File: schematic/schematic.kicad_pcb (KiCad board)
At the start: 4 copper layers, 100 x 100 mm, 260 parts, among them J1 Conn_01x04, J10 Conn_01x03, J11 Conn_01x02, J12 Conn_01x02, J13 Conn_01x02, J14 Conn_01x02, J15 Conn_01x02, J16 Conn_01x02, J17 Conn_01x04, J18 Conn_02x13_Odd_Even, J2 Conn_01x04, J3 Conn_01x04, J4 Conn_01x04, J5 Conn_01x04, J6 Conn_01x06, J7 Conn_01x03, J8 Screw_Terminal_01x02, J9 Conn_01x03, Q1 PSMN1R7-30YL, Q2 PSMN1R7-30YL, Q3 NCV8402, Q4 NCV8402, SW1 SW_Push_Dual, SW2 SW_DIP_x03, U1 STM32F401VETx, U2 TMC2130, U3 TMC2130, U4 TMC2130, U5 TMC2130, U6 BD9E302EFJ, U7 BD9E302EFJ, U8 BD9E302EFJ, Y1 Crystal_GND24

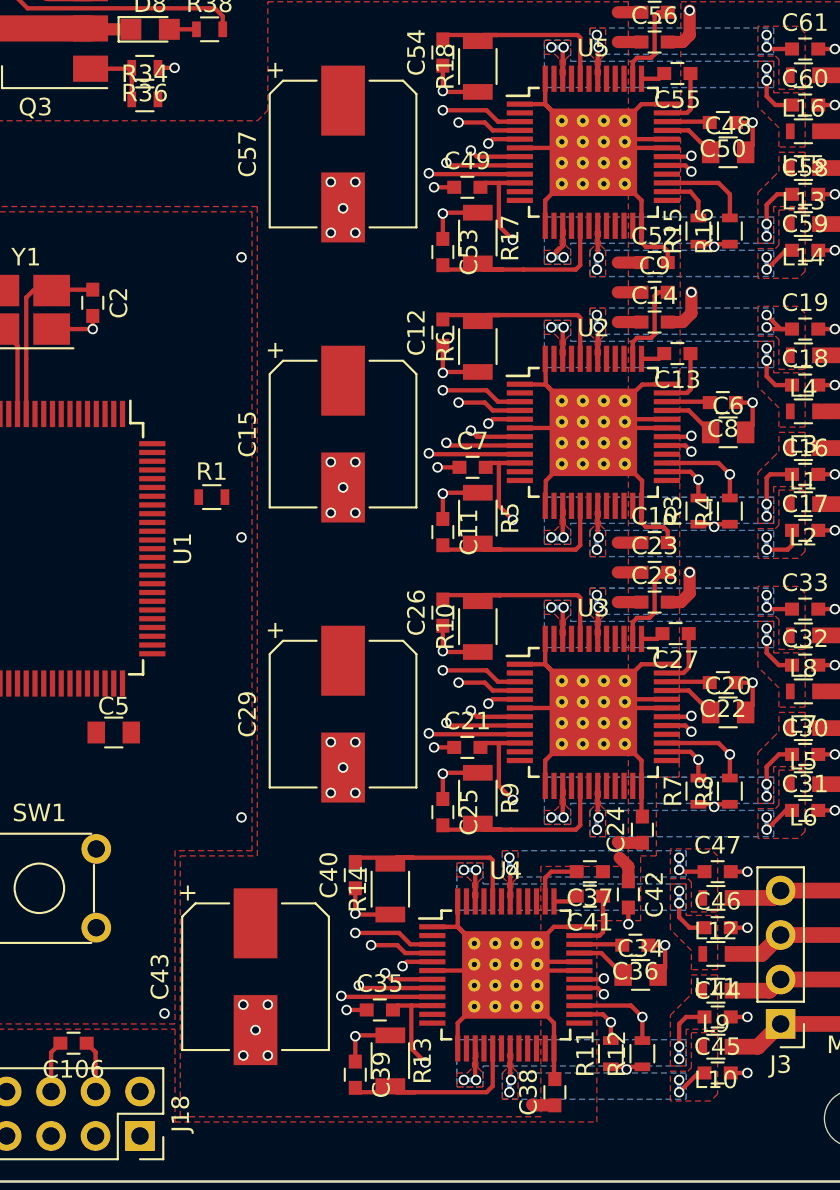
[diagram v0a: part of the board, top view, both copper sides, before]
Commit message: Routed signals to E driver
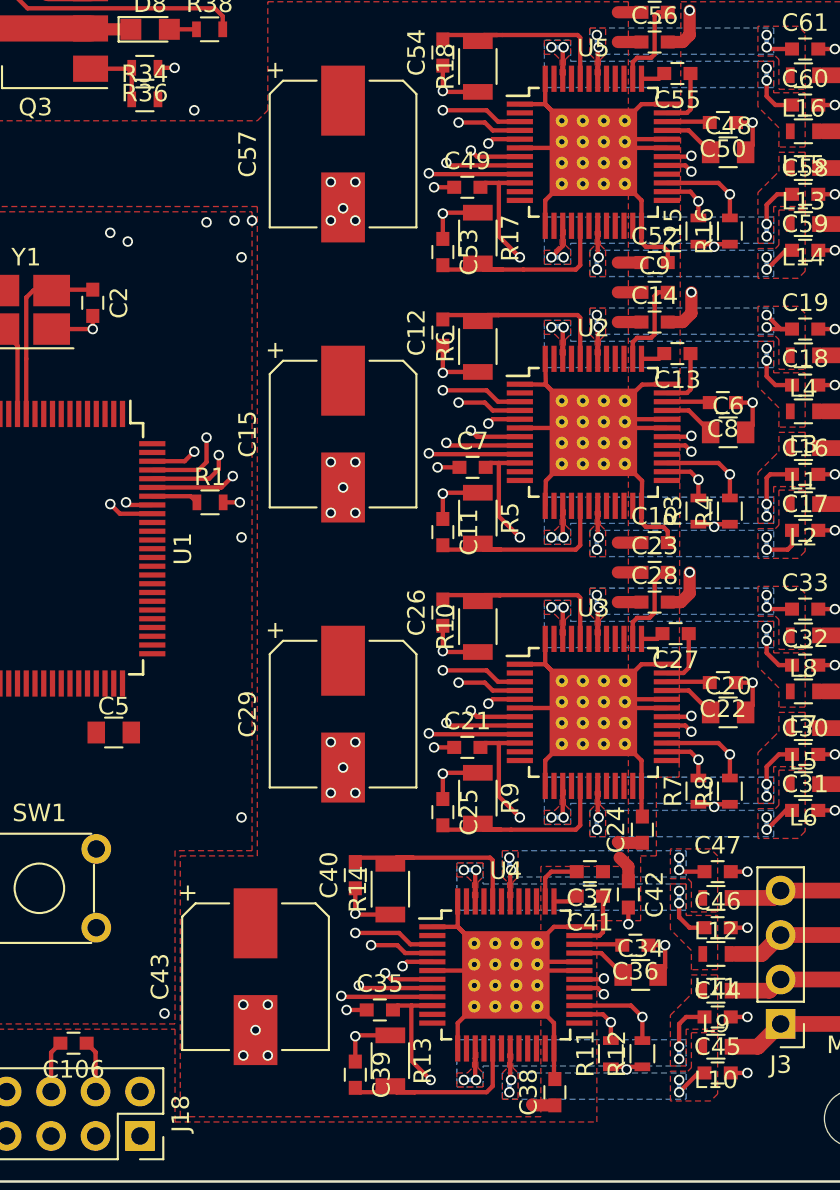
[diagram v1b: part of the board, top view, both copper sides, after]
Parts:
- moved R1 0.32 mm to (224.7, 111.2)
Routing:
- net ED0: track 3.01 -> 55.7 mm, vias 0 -> 3
- net ED1: track 5.22 -> 57.2 mm, vias 0 -> 3
- net ESS: track 4.67 -> 41.0 mm, vias 1 -> 3
- net ESTEP: track 4.26 -> 36.8 mm, vias 1 -> 3
- net EDIR: track 5.22 -> 36.5 mm, vias 1 -> 3
- net EEN: track 17.8 -> 48.4 mm, vias 1 -> 3
- net +3V3: track 144.6 -> 149.5 mm
- net BOOT0: track 0.00 -> 2.69 mm
- net GND: track 362.8 -> 362.6 mm, vias 110 -> 111

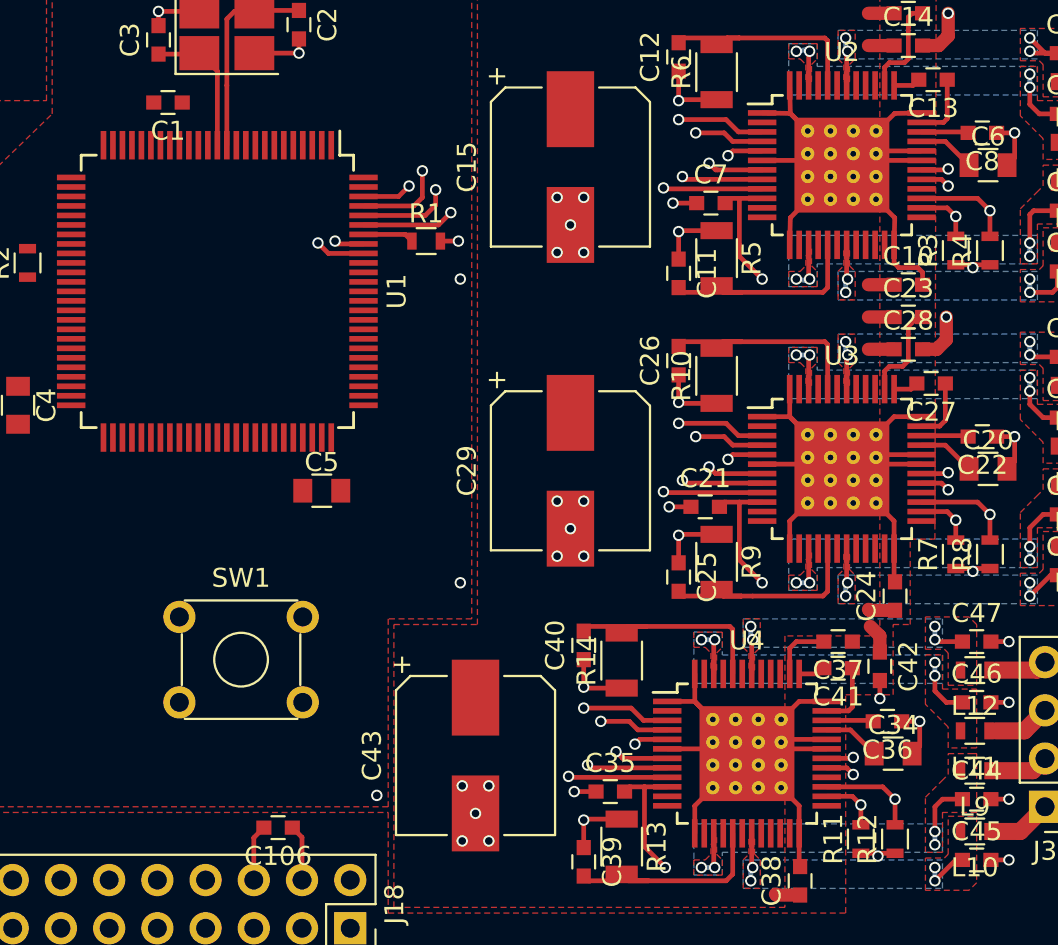
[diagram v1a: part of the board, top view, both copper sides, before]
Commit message: Routed all control signals to drivers
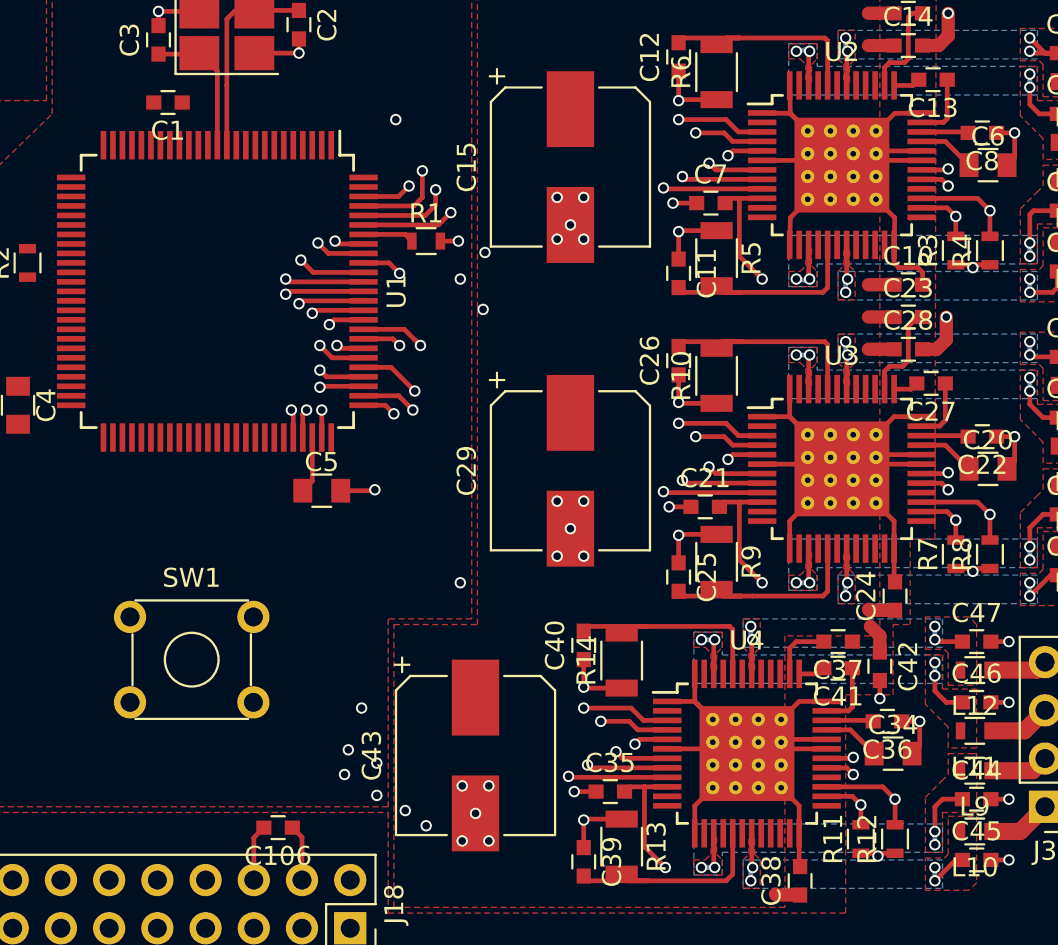
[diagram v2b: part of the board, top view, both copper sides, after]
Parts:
- moved SW1 2.60 mm to (209.1, 131.0)
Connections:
- U1 pad 80: YD0 -> YD1
- U1 pad 81: YD1 -> YD0
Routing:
- net ZD1: track 5.22 -> 60.6 mm, vias 1 -> 3
- net ZD0: track 3.04 -> 55.5 mm, vias 1 -> 3
- net ZEN: track 1.54 -> 51.6 mm, vias 1 -> 3
- net YD0: track 3.04 -> 46.1 mm, vias 1 -> 2
- net XD1: track 5.22 -> 47.1 mm, vias 1 -> 2
- net XEN: track 1.54 -> 43.2 mm, vias 1 -> 2
- net XD0: track 3.04 -> 43.7 mm, vias 1 -> 4
- net YD1: track 5.22 -> 45.3 mm, vias 1 -> 2
- net YEN: track 1.54 -> 41.0 mm, vias 1 -> 2
- net ZSTEP: track 4.26 -> 39.9 mm, vias 1 -> 3
- net ZSS: track 4.67 -> 38.5 mm, vias 1 -> 3
- net ZDIR: track 5.22 -> 37.9 mm, vias 1 -> 3
- net XSTEP: track 4.26 -> 34.8 mm, vias 1 -> 2
- net XDIR: track 5.22 -> 31.8 mm, vias 1 -> 2
- net XSS: track 4.67 -> 30.0 mm, vias 1 -> 3
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
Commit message: More routing done
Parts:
- moved R66 104.2 mm to (239.7, 153.9)
- moved R67 104.2 mm to (243.5, 153.9)
- moved R68 104.2 mm to (247.3, 163.9)
- moved R69 104.2 mm to (243.5, 163.9)
- moved R71 104.2 mm to (239.7, 163.9)
- moved R74 104.2 mm to (239.5, 158.9)
- moved R70 104.2 mm to (246.3, 158.9)
- moved R72 104.2 mm to (247.1, 153.9)
- moved R73 104.2 mm to (242.8, 158.9)
- moved C100 104.2 mm to (231.5, 153.9)
- moved C101 104.2 mm to (235.7, 153.9)
- moved C102 104.2 mm to (231.5, 159.2)
- moved C103 104.2 mm to (227.2, 153.9)
- moved C104 104.2 mm to (227.2, 159.2)
- moved C105 104.2 mm to (235.7, 159.2)
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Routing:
- net BOOT0: track 2.69 -> 49.0 mm, vias 0 -> 3
- net MISO: track 56.5 -> 96.8 mm, vias 4 -> 7
- net MOSI: track 60.7 -> 98.1 mm, vias 4 -> 7
- net SCK: track 63.8 -> 100.8 mm, vias 4 -> 7
- net TX: track 0.00 -> 25.7 mm, vias 0 -> 1
- net RX: track 0.00 -> 25.0 mm, vias 0 -> 1
- net GND: track 364.7 -> 373.6 mm, vias 113 -> 118
- net Net-(C4-Pad1): track 0.00 -> 2.80 mm
- net BOOT1: track 0.00 -> 2.07 mm

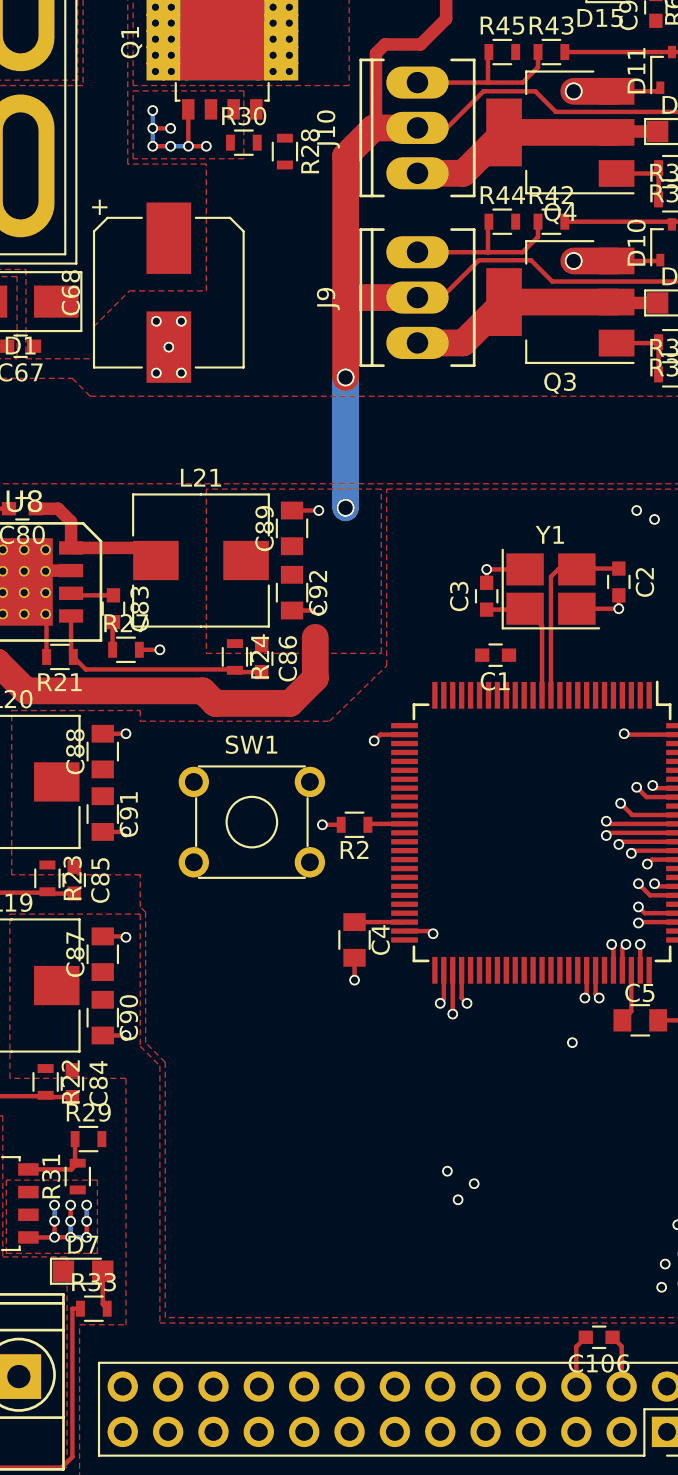
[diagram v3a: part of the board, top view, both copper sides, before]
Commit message: Added display headers
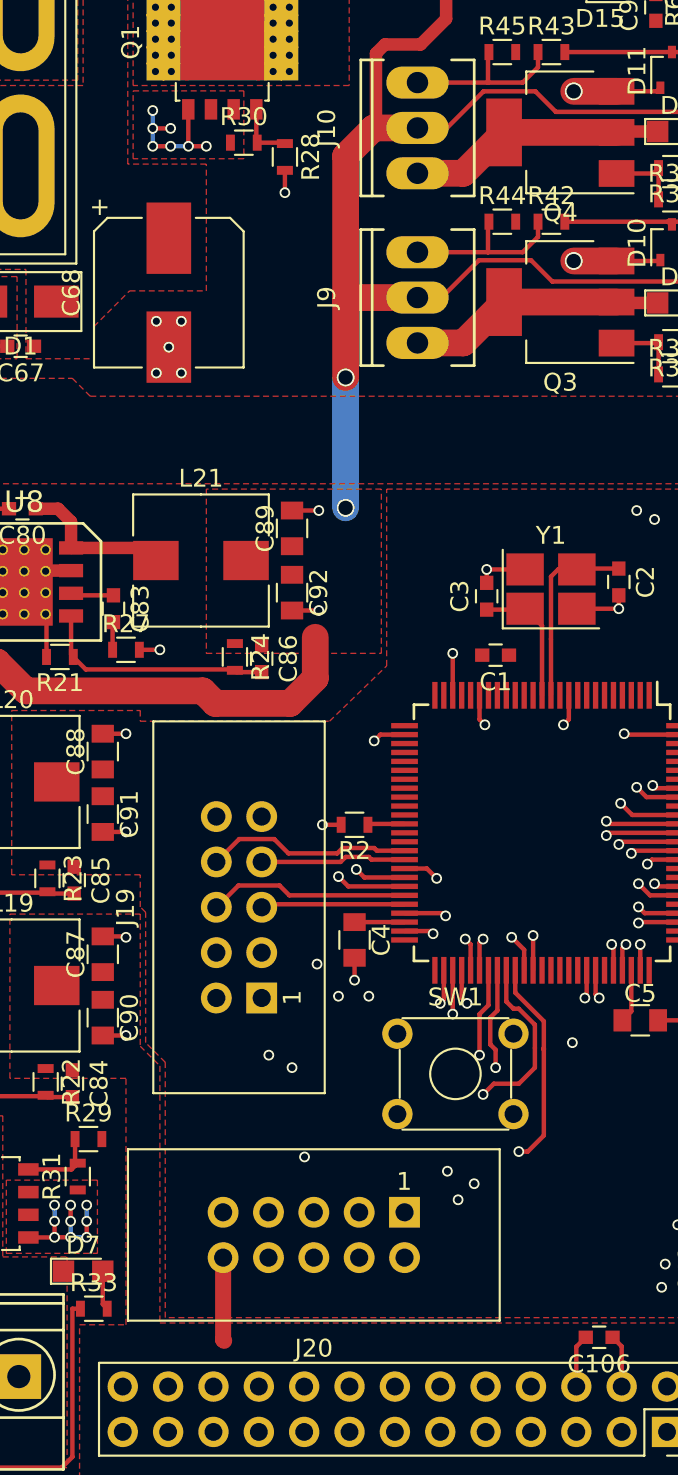
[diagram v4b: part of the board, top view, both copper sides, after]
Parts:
- added J19: Conn_02x05_Odd_Even, Connectors:IDC_Header_Straight_10pins, F.Cu at (198.0, 123.1)
- added J20: Conn_02x05_Odd_Even, Connectors:IDC_Header_Straight_10pins, F.Cu at (206.0, 135.1)
- moved SW1 18.1 mm to (205.6, 125.1)
- moved R28 0.30 mm to (199.3, 76.0)
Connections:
- U1 pad 40: Net-(U1-Pad40) -> RESET
- U1 pad 41: Net-(U1-Pad41) -> SDDETECT
- U1 pad 42: Net-(U1-Pad42) -> SDSS
- U1 pad 43: Net-(U1-Pad43) -> SDCLK
- U1 pad 44: Net-(U1-Pad44) -> SDMISO
- U1 pad 45: Net-(U1-Pad45) -> SDMOSI
- U1 pad 46: Net-(U1-Pad46) -> ENC3
- U1 pad 47: Net-(U1-Pad47) -> ENC2
- U1 pad 55: Net-(U1-Pad55) -> LCD4
- U1 pad 56: Net-(U1-Pad56) -> LCD5
- U1 pad 57: Net-(U1-Pad57) -> LCD6
- U1 pad 58: Net-(U1-Pad58) -> LCD7
- U1 pad 59: Net-(U1-Pad59) -> LCDRS
- U1 pad 60: Net-(U1-Pad60) -> LCDE
- U1 pad 61: Net-(U1-Pad61) -> BEEP
- U1 pad 62: Net-(U1-Pad62) -> ENC1
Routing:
- net BPWM: track 0.00 -> 36.9 mm, vias 0 -> 2
- net LCD5: track 0.00 -> 29.8 mm, vias 0 -> 3
- net LCD7: track 0.00 -> 28.3 mm, vias 0 -> 2
- net LCDRS: track 0.00 -> 26.5 mm, vias 0 -> 1
- net LCD6: track 0.00 -> 25.6 mm, vias 0 -> 2
- net ENC1: track 0.00 -> 25.1 mm, vias 0 -> 1
- net BEEP: track 0.00 -> 24.2 mm, vias 0 -> 1
- net LCD4: track 0.00 -> 23.7 mm, vias 0 -> 1
- net LCDE: track 0.00 -> 23.4 mm, vias 0 -> 1
- net SDCLK: track 0.00 -> 20.0 mm, vias 0 -> 2
- net SDSS: track 0.00 -> 16.1 mm, vias 0 -> 1
- net SDMISO: track 0.00 -> 15.0 mm, vias 0 -> 2
- net ENC2: track 0.00 -> 13.5 mm, vias 0 -> 1
- net RESET: track 0.00 -> 11.6 mm
- net SDMOSI: track 0.00 -> 11.3 mm
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
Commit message: 3.3V to upper area of the board
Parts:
- moved R69 88.9 mm to (257.9, 76.2), turned to 90 degrees
- moved R71 88.7 mm to (253.0, 76.2), turned to 90 degrees
- moved R68 87.7 mm to (249.6, 76.2), turned to 270 degrees
- moved C104 86.1 mm to (262.0, 80.5), turned to 180 degrees
- moved C102 85.4 mm to (251.3, 76.2), turned to 270 degrees
- moved R70 84.3 mm to (262.8, 76.2), turned to 90 degrees
- moved R73 82.4 mm to (262.0, 78.8), turned to 180 degrees
- moved C101 81.8 mm to (261.1, 76.2), turned to 270 degrees
- moved C100 81.6 mm to (256.2, 76.2), turned to 270 degrees
- moved R74 81.1 mm to (252.2, 78.8), turned to 180 degrees
- moved C105 80.4 mm to (252.2, 80.5), turned to 180 degrees
- moved R67 79.3 mm to (259.4, 76.2), turned to 270 degrees
- moved C103 79.3 mm to (257.1, 80.5), turned to 180 degrees
- moved R66 79.1 mm to (254.5, 76.2), turned to 270 degrees
- moved R72 75.8 mm to (257.1, 78.8), turned to 180 degrees
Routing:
- net /AREF/Z-REF: track 1.42 -> 76.5 mm, vias 1 -> 2
- net /AREF/XY-REF: track 2.84 -> 65.8 mm, vias 2 -> 3
- net /AREF/E-REF: track 1.42 -> 18.0 mm, vias 1 -> 2
- net /AREF/Z-PWM: track 0.00 -> 15.5 mm, vias 0 -> 2
- net GND: track 377.2 -> 390.1 mm, vias 120 -> 123
- net /AREF/XY-PWM: track 0.00 -> 10.6 mm, vias 0 -> 2
- net +3V3: track 149.5 -> 156.8 mm, vias 12 -> 14
- net /AREF/E-PWM: track 0.00 -> 5.61 mm, vias 0 -> 2
- net Net-(C101-Pad1): track 0.00 -> 3.61 mm
- net Net-(C102-Pad1): track 0.00 -> 3.61 mm
- net Net-(C100-Pad1): track 0.00 -> 3.61 mm

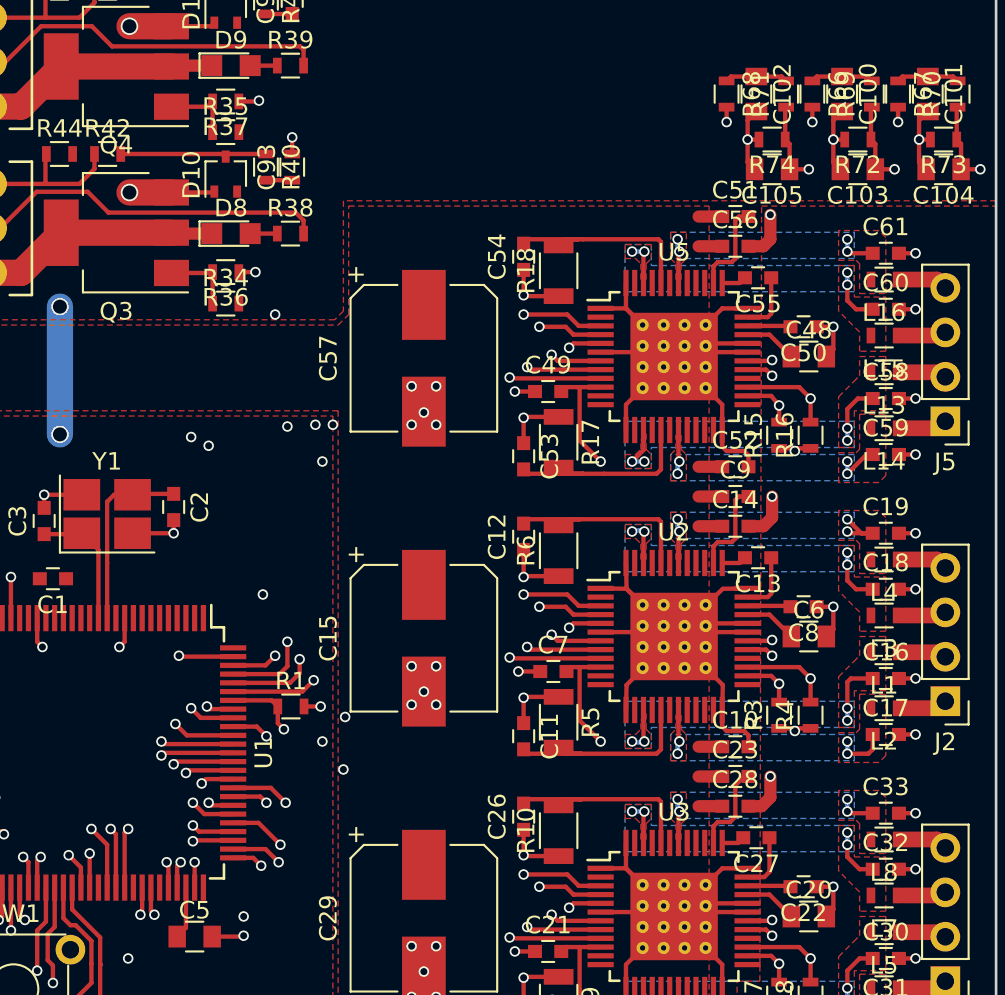
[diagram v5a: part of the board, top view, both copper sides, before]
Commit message: Routed current pwm drivers
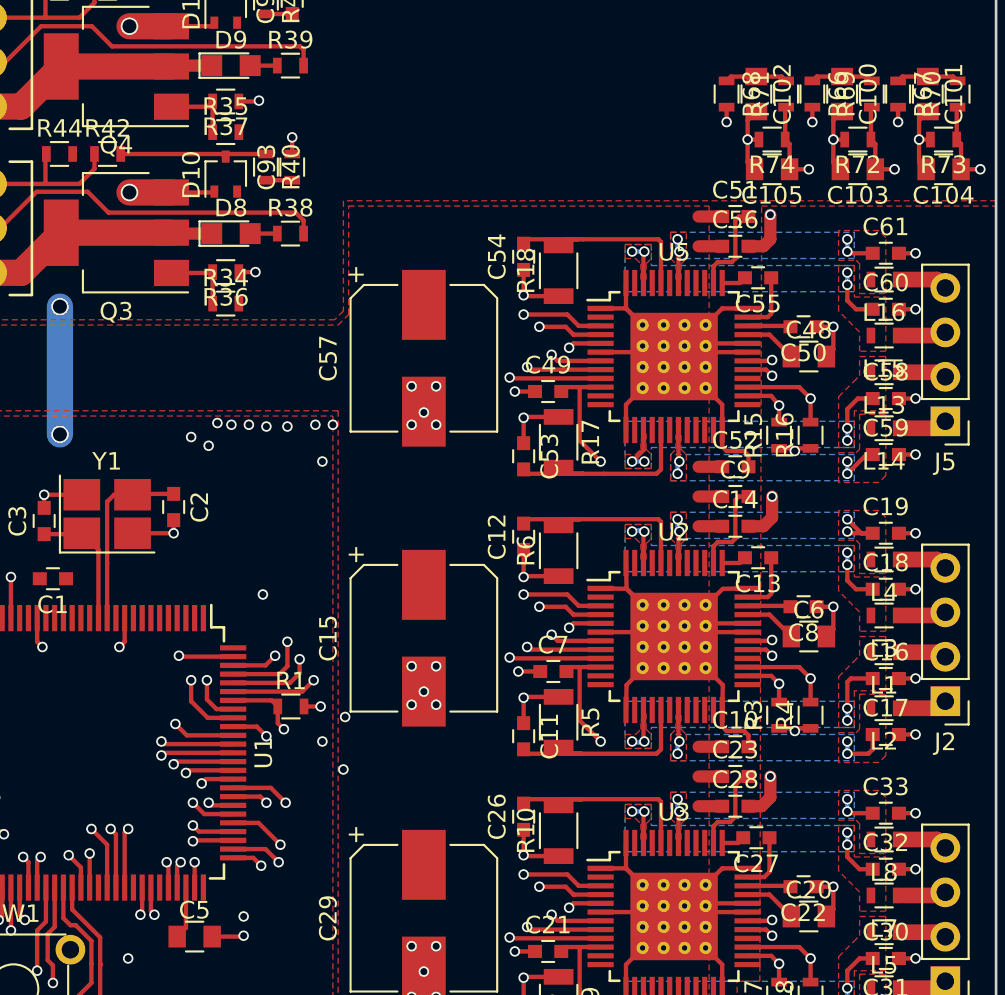
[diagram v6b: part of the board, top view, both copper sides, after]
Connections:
- U1 pad 64: /AREF/XY-PWM -> /AREF/E-PWM
- U1 pad 65: /AREF/Z-PWM -> /AREF/XY-PWM
- U1 pad 66: /AREF/E-PWM -> /AREF/Z-PWM
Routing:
- net /AREF/E-PWM: track 5.61 -> 70.5 mm, vias 2 -> 3
- net /AREF/XY-PWM: track 10.6 -> 73.0 mm, vias 2 -> 3
- net /AREF/Z-PWM: track 15.5 -> 76.5 mm, vias 2 -> 3
- net +3V3: track 156.8 -> 149.5 mm, vias 14 -> 12
- net (no net): track 0.00 -> 7.30 mm, vias 0 -> 2
- net ESS: track 41.0 -> 38.0 mm
